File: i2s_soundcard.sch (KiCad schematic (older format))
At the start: 13 parts, among them J1 Conn_01x08, J2 Conn_01x06, J3 Conn_01x05, J4 Conn_01x11, J5 Conn_01x04, U1 TLV320AIC3104IRHBT, U6 TLV7111830DSER, U7 TPD4E02B04DQAR, U8 TPD4E02B04DQAR

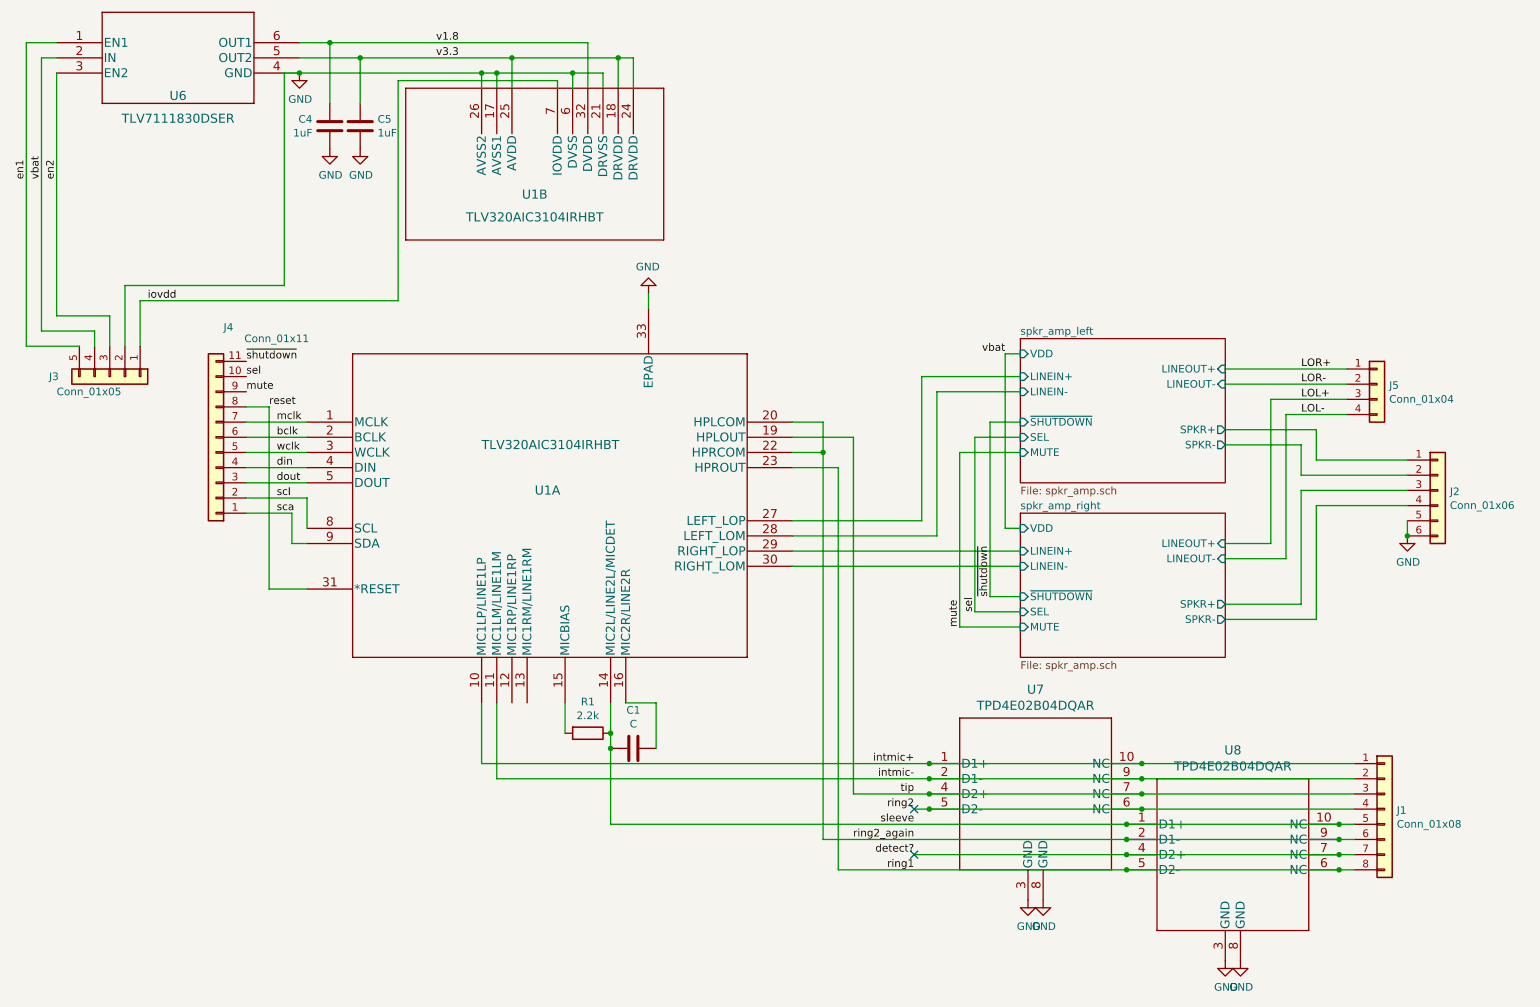
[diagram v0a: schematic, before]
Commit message: Fix ERC errors by adjusting pin types and adding power flags as necessary.
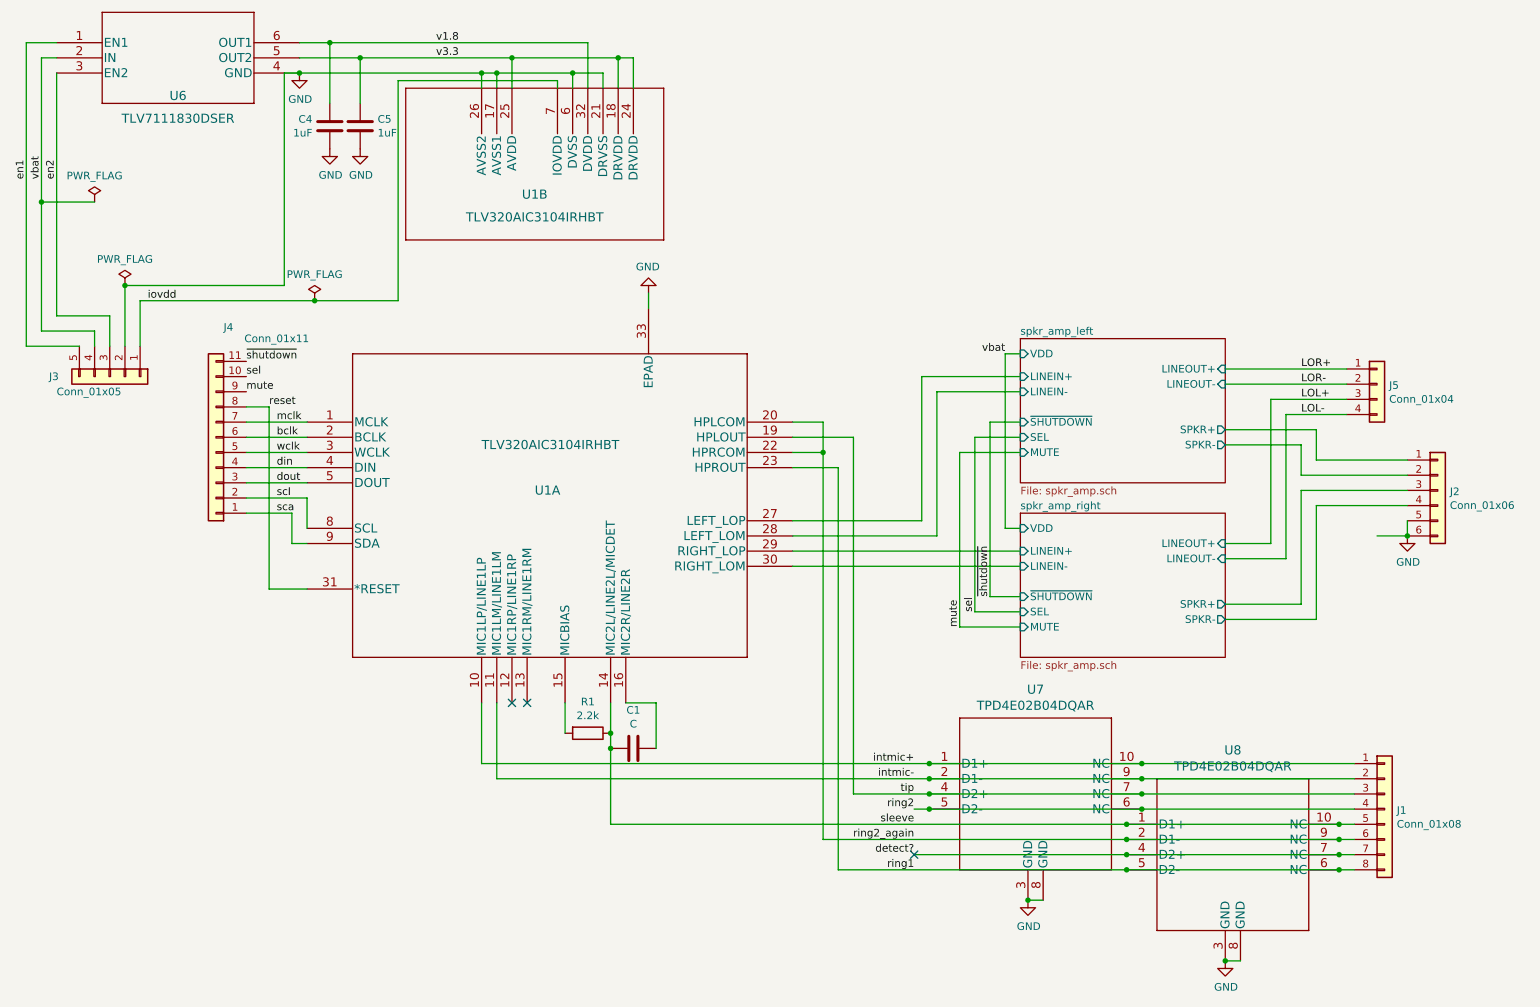
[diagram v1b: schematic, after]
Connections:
- no-connect marks 2 -> 3
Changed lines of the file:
@@
 Wire Wire Line
 	4850 5400 4850 5900
-NoConn ~ 6850 5800
 NoConn ~ 6850 6100
 $Comp
@@
 Wire Wire Line
 	1450 2650 1100 2650
-Wire Wire Line
-	1100 2650 1100 850
 Wire Wire Line
 	1100 850  1200 850
@@
 	1750 2750 1750 2450
 Wire Wire Line
-	1750 2450 3450 2450
+	1750 2450 2900 2450
 $Comp
 L TPD4E02B04DQAR:TPD4E02B04DQAR U7
@@
 	6450 5700 6950 5700
 Wire Wire Line
-	6850 5800 6950 5800
-Wire Wire Line
 	4850 5900 8250 5900
 Wire Wire Line
@@
 $EndComp
 $Comp
-L power:GND #PWR0107
-U 1 1 6055B087
-P 9000 6800
-F 0 "#PWR0107" H 9000 6550 50  0001 C CNN
-F 1 "GND" H 9005 6627 50  0000 C CNN
-F 2 "" H 9000 6800 50  0001 C CNN
-F 3 "" H 9000 6800 50  0001 C CNN
-	1    9000 6800
-	1    0    0    -1
-$EndComp
-$Comp
-L power:GND #PWR0108
-U 1 1 6055B29C
-P 7700 6400
-F 0 "#PWR0108" H 7700 6150 50  0001 C CNN
-F 1 "GND" H 7705 6227 50  0000 C CNN
-F 2 "" H 7700 6400 50  0001 C CNN
-F 3 "" H 7700 6400 50  0001 C CNN
-	1    7700 6400
-	1    0    0    -1
-$EndComp
-$Comp
 L power:GND #PWR0109
 U 1 1 6055B7F2
@@
 	8350 5800 6950 5800
 Connection ~ 8350 5800
-Connection ~ 6950 5800
 Wire Wire Line
 	6950 5700 8350 5700
@@
 Text Label 6850 6100 2    50   ~ 0
 detect?
+Wire Wire Line
+	7600 6400 7700 6400
+Connection ~ 7600 6400
+Wire Wire Line
+	8900 6800 9000 6800
+Connection ~ 8900 6800
+$Comp
+L power:PWR_FLAG #FLG0101
+U 1 1 6060E57E
+P 1650 2350
+F 0 "#FLG0101" H 1650 2425 50  0001 C CNN
+F 1 "PWR_FLAG" H 1650 2523 50  0000 C CNN
+F 2 "" H 1650 2350 50  0001 C CNN
+F 3 "~" H 1650 2350 50  0001 C CNN
+	1    1650 2350
+	1    0    0    -1
+$EndComp
+Wire Wire Line
+	9900 4000 10100 4000
+Connection ~ 1650 2350
+$Comp
+L power:PWR_FLAG #FLG0102
+U 1 1 60615D2D
+P 1450 1800
+F 0 "#FLG0102" H 1450 1875 50  0001 C CNN
+F 1 "PWR_FLAG" H 1450 1973 50  0000 C CNN
+F 2 "" H 1450 1800 50  0001 C CNN
+F 3 "~" H 1450 1800 50  0001 C CNN
+	1    1450 1800
+	1    0    0    -1
+$EndComp
+Wire Wire Line
+	1100 2650 1100 1800
+Wire Wire Line
+	1450 1800 1100 1800
+Connection ~ 1100 1800
+Wire Wire Line
+	1100 1800 1100 850
+NoConn ~ 4200 5100
+NoConn ~ 4300 5100
+$Comp
+L power:PWR_FLAG #FLG0103
+U 1 1 6062ECA7
+P 2900 2450
+F 0 "#FLG0103" H 2900 2525 50  0001 C CNN
+F 1 "PWR_FLAG" H 2900 2623 50  0000 C CNN
+F 2 "" H 2900 2450 50  0001 C CNN
+F 3 "~" H 2900 2450 50  0001 C CNN
+	1    2900 2450
+	1    0    0    -1
+$EndComp
+Connection ~ 2900 2450
+Wire Wire Line
+	2900 2450 3450 2450
+Wire Wire Line
+	6850 5800 6950 5800
+Connection ~ 6950 5800
 $EndSCHEMATC
